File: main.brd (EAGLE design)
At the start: 81.3 x 100 mm, 8 parts, among them X1 FH12-40S-0.5SH

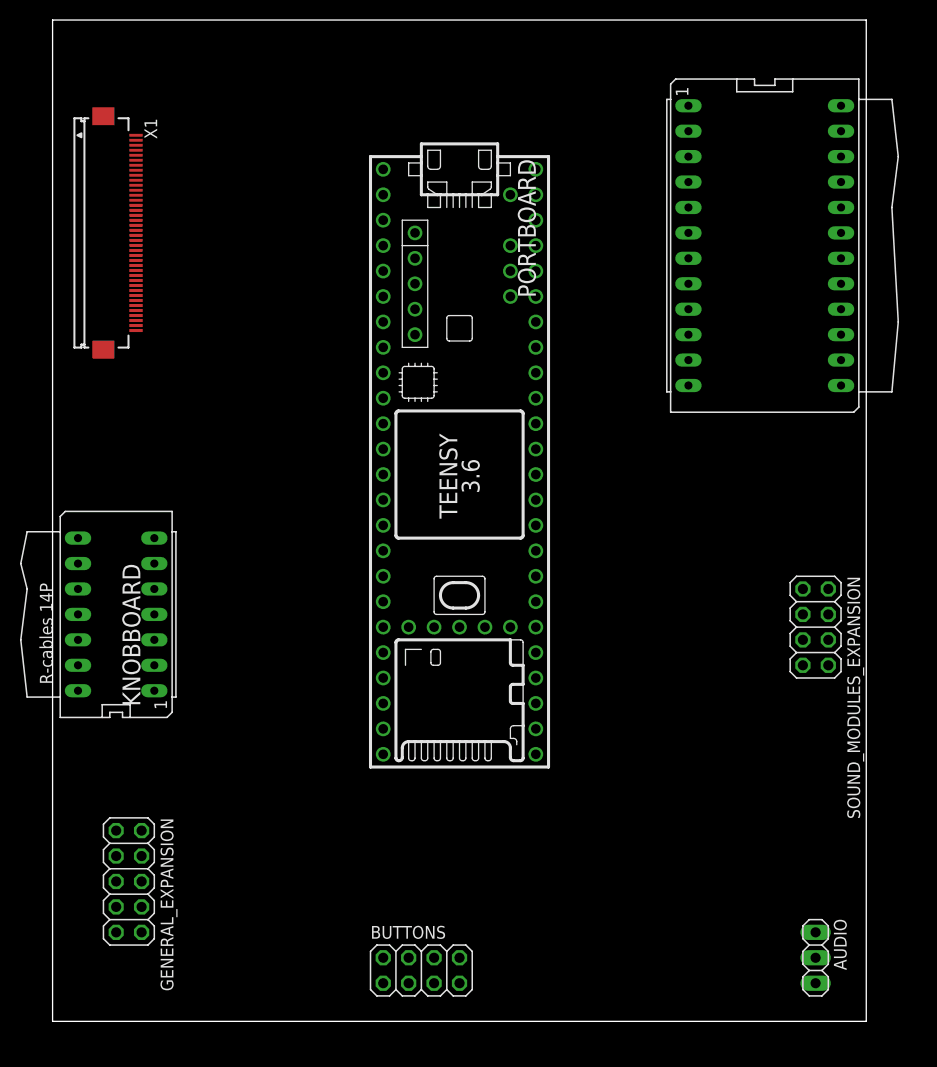
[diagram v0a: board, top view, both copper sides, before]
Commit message: pcb cleanup and audio_main tidy
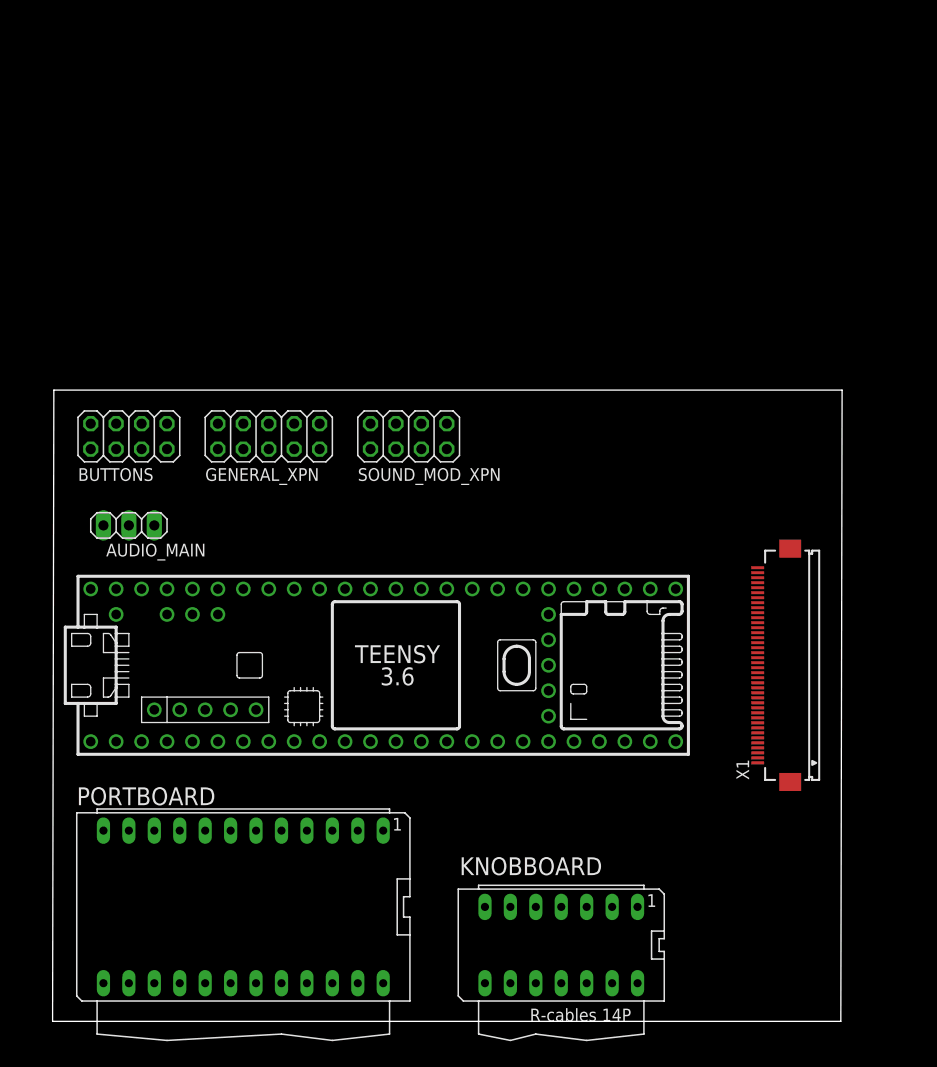
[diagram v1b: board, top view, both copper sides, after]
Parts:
- removed AUDIO: (no value), pinhead:1X03
- removed GENERAL_EXPANSION: (no value), pinhead:2X05
- removed SOUND_MODULES_EXPANSION: (no value), pinhead:2X04
- added AUDIO_MAIN: (no value), pinhead:1X03
- added GENERAL_XPN: (no value), pinhead:2X05
- added SOUND_MOD_XPN: (no value), pinhead:2X04
- moved PORTBOARD 84.1 mm to (19.1, 11.4), turned to 180 degrees
- moved X1 81.0 mm to (73.7, 35.6), turned to 90 degrees
- moved BUTTONS 60.8 mm to (7.62, 58.4)
- moved KNOBBOARD 55.4 mm to (50.8, 7.62), turned to 180 degrees
- moved U$1 23.3 mm to (31.8, 35.6), turned to 0 degrees
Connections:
- net AUDIO_GND: now also AUDIO_MAIN.2; no longer AUDIO.2
- net AUDIO_L: now also AUDIO_MAIN.1; no longer AUDIO.3
- net AUDIO_R: now also AUDIO_MAIN.3; no longer AUDIO.1
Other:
- board size 81.3 x 100 mm -> 78.8 x 63 mm

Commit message: general expansion slots
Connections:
- net N$10 renamed MIDIIN3
- net N$11 renamed MIDIIN4
- net N$12 renamed SDDATA1
- net N$3 renamed MIDIOUT1
- net N$4 renamed MIDIOUT2
- net N$5 renamed MIDIOUT3
- net N$6 renamed MIDIOUT4
- net N$7 renamed SDDATA0
- net N$8 renamed MIDIIN1
- net N$9 renamed MIDIIN2
- new net +12V: GENERAL_XPN.3
- new net BUTTON_CLK: BUTTONS.7
- new net BUTTON_DATA: BUTTONS.6
- new net BUTTON_S/P: BUTTONS.5
- new net LEDSCL: BUTTONS.4
- new net LED_SDA: BUTTONS.3
- new net SDCLK: PORTBOARD.9
- new net SDCMD: PORTBOARD.16
- new net SDDATA2: PORTBOARD.8
- new net SDDATA3: PORTBOARD.17
- new net SPI_CLK: GENERAL_XPN.8
- new net SPI_CS: GENERAL_XPN.7
- new net SPI_MISO: GENERAL_XPN.10
- new net SPI_MOSI: GENERAL_XPN.9
- net +3V3: now also BUTTONS.1
- net +5V: now also GENERAL_XPN.1
- net AUDIO_L: now also GENERAL_XPN.5
- net AUDIO_R: now also GENERAL_XPN.6
- net GND: now also BUTTONS.2, GENERAL_XPN.2
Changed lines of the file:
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@@
 <contactref element="PORTBOARD" pad="1"/>
 <contactref element="PORTBOARD" pad="2"/>
-<wire x1="70.41" y1="25.81" x2="58.42" y2="3.81" width="0" layer="19" extent="1-1"/>
-<wire x1="33.02" y1="19.05" x2="70.41" y2="25.81" width="0" layer="19" extent="1-1"/>
+<contactref element="BUTTONS" pad="2"/>
+<contactref element="GENERAL_XPN" pad="2"/>
+<wire x1="58.42" y1="3.81" x2="70.41" y2="25.81" width="0" layer="19" extent="1-1"/>
+<wire x1="33.02" y1="19.05" x2="58.42" y2="3.81" width="0" layer="19" extent="1-1"/>
 <wire x1="30.48" y1="19.05" x2="33.02" y2="19.05" width="0" layer="19" extent="1-1"/>
 <wire x1="3.81" y1="27.94" x2="30.48" y2="19.05" width="0" layer="19" extent="1-1"/>
+<wire x1="3.81" y1="59.69" x2="3.81" y2="27.94" width="0" layer="19" extent="1-1"/>
+<wire x1="16.51" y1="59.69" x2="3.81" y2="59.69" width="0" layer="19" extent="1-1"/>
 </signal>
 <signal name="+3V3">
 <contactref element="X1" pad="2"/>
-<contactref element="U$1" pad="3V3"/>
 <contactref element="KNOBBOARD" pad="1"/>
 <contactref element="PORTBOARD" pad="24"/>
-<wire x1="70.41" y1="26.31" x2="58.42" y2="11.43" width="0" layer="19" extent="1-1"/>
-<wire x1="33.02" y1="3.81" x2="70.41" y2="26.31" width="0" layer="19" extent="1-1"/>
-<wire x1="39.37" y1="27.94" x2="70.41" y2="26.31" width="0" layer="19" extent="1-1"/>
+<contactref element="U$1" pad="3V3"/>
+<contactref element="BUTTONS" pad="1"/>
+<wire x1="58.42" y1="11.43" x2="70.41" y2="26.31" width="0" layer="19" extent="1-1"/>
+<wire x1="39.37" y1="27.94" x2="58.42" y2="11.43" width="0" layer="19" extent="1-1"/>
+<wire x1="33.02" y1="3.81" x2="39.37" y2="27.94" width="0" layer="19" extent="1-1"/>
+<wire x1="3.81" y1="57.15" x2="39.37" y2="27.94" width="0" layer="19" extent="1-1"/>
 </signal>
 <signal name="+5V">
 <contactref element="U$1" pad="VIN"/>
 <contactref element="PORTBOARD" pad="23"/>
+<contactref element="GENERAL_XPN" pad="1"/>
+<wire x1="3.81" y1="43.18" x2="16.51" y2="57.15" width="0" layer="19" extent="1-1"/>
 <wire x1="30.48" y1="3.81" x2="3.81" y2="43.18" width="0" layer="19" extent="1-1"/>
 </signal>
@@
 <contactref element="U$1" pad="A22/DAC1"/>
 <contactref element="AUDIO_MAIN" pad="3"/>
-<wire x1="5.08" y1="49.53" x2="41.91" y2="43.18" width="0" layer="19" extent="1-1"/>
+<contactref element="GENERAL_XPN" pad="6"/>
+<wire x1="21.59" y1="59.69" x2="41.91" y2="43.18" width="0" layer="19" extent="1-1"/>
+<wire x1="5.08" y1="49.53" x2="21.59" y2="59.69" width="0" layer="19" extent="1-1"/>
 </signal>
 <signal name="AUDIO_L">
 <contactref element="U$1" pad="21/DAC0"/>
 <contactref element="AUDIO_MAIN" pad="1"/>
-<wire x1="10.16" y1="49.53" x2="44.45" y2="43.18" width="0" layer="19" extent="1-1"/>
+<contactref element="GENERAL_XPN" pad="5"/>
+<wire x1="21.59" y1="57.15" x2="44.45" y2="43.18" width="0" layer="19" extent="1-1"/>
+<wire x1="10.16" y1="49.53" x2="21.59" y2="57.15" width="0" layer="19" extent="1-1"/>
 </signal>
 <signal name="AUDIO_GND">
@@
 <wire x1="6.35" y1="43.18" x2="7.62" y2="49.53" width="0" layer="19" extent="1-1"/>
 </signal>
-<signal name="N$3">
+<signal name="MIDIOUT1">
 <contactref element="PORTBOARD" pad="3"/>
 </signal>
-<signal name="N$4">
+<signal name="MIDIOUT2">
 <contactref element="PORTBOARD" pad="4"/>
 </signal>
-<signal name="N$5">
+<signal name="MIDIOUT3">
 <contactref element="PORTBOARD" pad="5"/>
 </signal>
-<signal name="N$6">
+<signal name="MIDIOUT4">
 <contactref element="PORTBOARD" pad="6"/>
 </signal>
-<signal name="N$7">
+<signal name="SDDATA0">
 <contactref element="PORTBOARD" pad="7"/>
 </signal>
-<signal name="N$8">
+<signal name="MIDIIN1">
 <contactref element="PORTBOARD" pad="22"/>
 </signal>
-<signal name="N$9">
+<signal name="MIDIIN2">
 <contactref element="PORTBOARD" pad="21"/>
 </signal>
-<signal name="N$10">
+<signal name="MIDIIN3">
 <contactref element="PORTBOARD" pad="20"/>
 </signal>
-<signal name="N$11">
+<signal name="MIDIIN4">
 <contactref element="PORTBOARD" pad="19"/>
 </signal>
-<signal name="N$12">
+<signal name="SDDATA1">
 <contactref element="PORTBOARD" pad="18"/>
 </signal>
+<signal name="SDDATA2">
+<contactref element="PORTBOARD" pad="8"/>
+</signal>
+<signal name="SDCLK">
+<contactref element="PORTBOARD" pad="9"/>
+</signal>
+<signal name="SDDATA3">
+<contactref element="PORTBOARD" pad="17"/>
+</signal>
+<signal name="SDCMD">
+<contactref element="PORTBOARD" pad="16"/>
+</signal>
+<signal name="LED_SDA">
+<contactref element="BUTTONS" pad="3"/>
+</signal>
+<signal name="BUTTON_S/P">
+<contactref element="BUTTONS" pad="5"/>
+</signal>
+<signal name="BUTTON_CLK">
+<contactref element="BUTTONS" pad="7"/>
+</signal>
+<signal name="LEDSCL">
+<contactref element="BUTTONS" pad="4"/>
+</signal>
+<signal name="BUTTON_DATA">
+<contactref element="BUTTONS" pad="6"/>
+</signal>
+<signal name="SPI_CS">
+<contactref element="GENERAL_XPN" pad="7"/>
+</signal>
+<signal name="SPI_CLK">
+<contactref element="GENERAL_XPN" pad="8"/>
+</signal>
+<signal name="SPI_MOSI">
+<contactref element="GENERAL_XPN" pad="9"/>
+</signal>
+<signal name="SPI_MISO">
+<contactref element="GENERAL_XPN" pad="10"/>
+</signal>
+<signal name="+12V">
+<contactref element="GENERAL_XPN" pad="3"/>
+</signal>
 </signals>

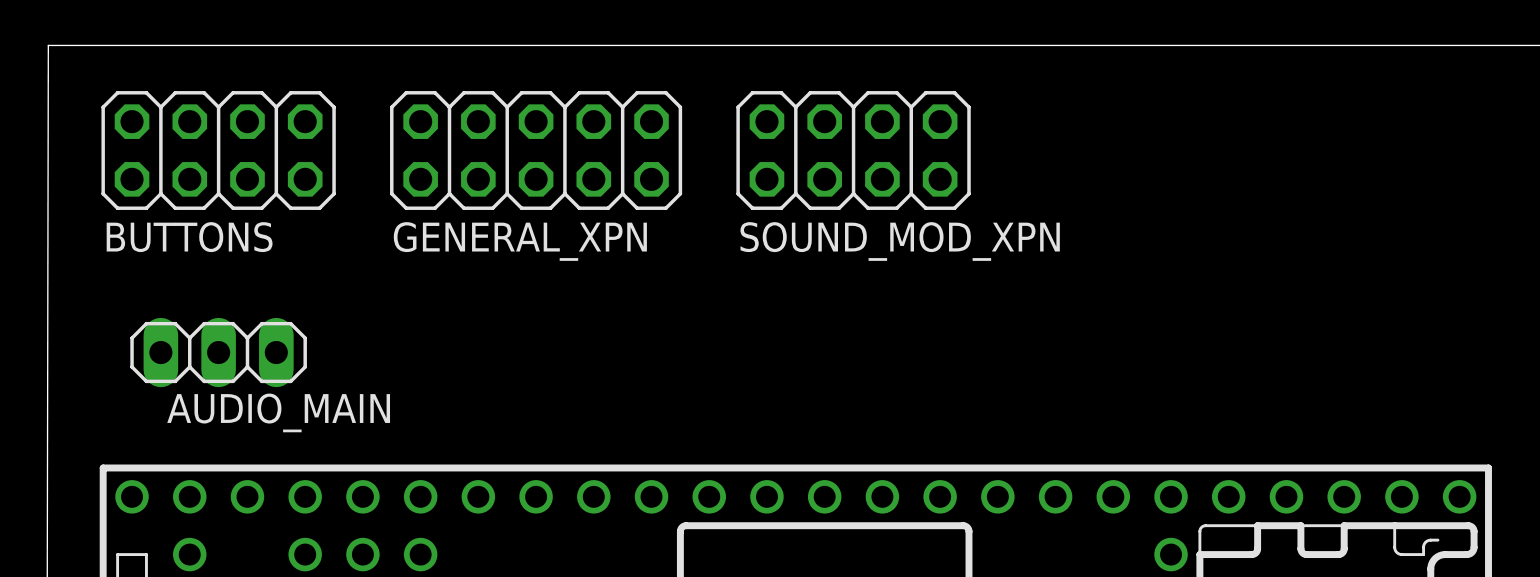
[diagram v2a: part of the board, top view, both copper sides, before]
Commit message: MIDI pinout connections, backup files cleanup, gitignore
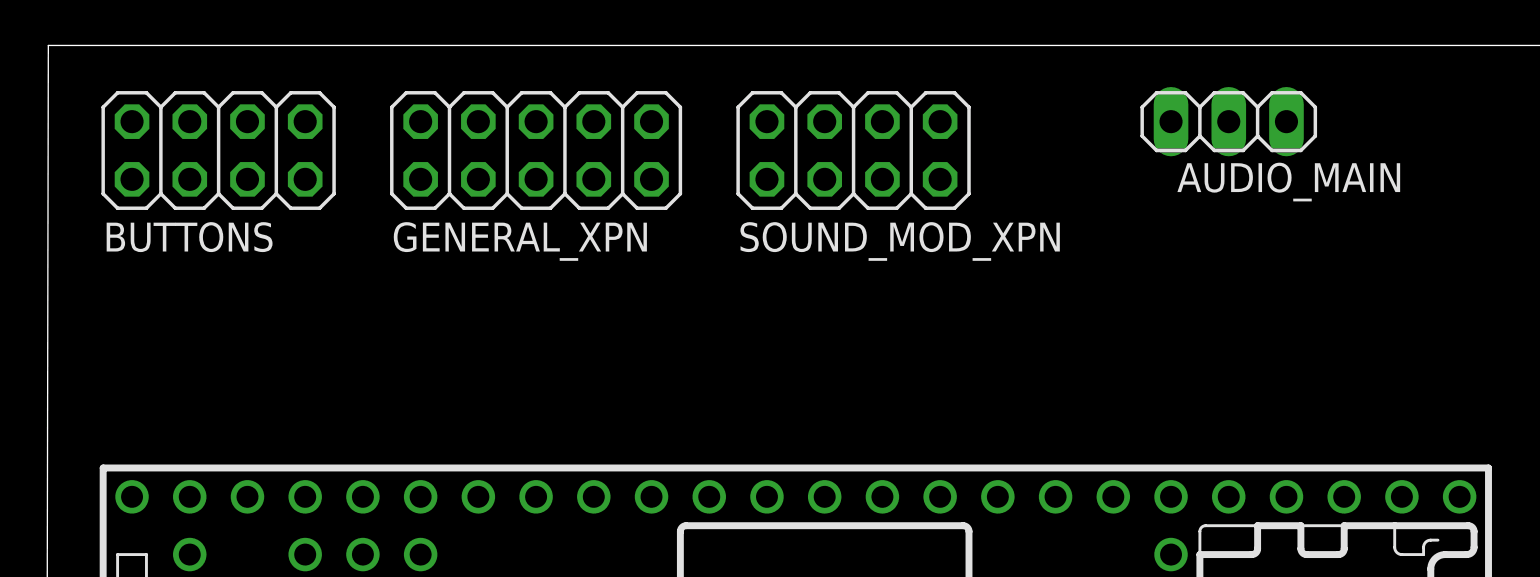
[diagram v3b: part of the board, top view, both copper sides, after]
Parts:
- moved AUDIO_MAIN 45.6 mm to (52.1, 59.7)
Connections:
- new net N$10: U$1.25
- new net N$11: U$1.26
- new net N$12: U$1.27
- new net N$13: U$1.28
- new net N$14: U$1.29
- new net N$15: U$1.30
- new net N$18: U$1.23/A9
- new net N$19: U$1.22/A8
- new net N$20: U$1.21/A7
- new net N$21: U$1.20/A6
- new net N$22: U$1.19/A5/SCL
- new net N$23: U$1.18/A4/SDA
- new net N$24: U$1.17/A3
- new net N$25: U$1.15/A1
- new net N$26: U$1.14/A0
- new net N$3: U$1.2
- new net N$30: U$1.35/A16
- new net N$31: U$1.36/A17
- new net N$32: U$1.37/A18
- new net N$33: U$1.38/A19
- new net N$34: U$1.39/A20
- new net N$4: U$1.3/CANTX
- new net N$5: U$1.4/CANRX
- new net N$6: U$1.6
- new net N$9: U$1.24
- net MIDIIN1: now also U$1.0/RX
- net MIDIIN2: now also U$1.7
- net MIDIIN3: now also U$1.31/A12
- net MIDIIN4: now also U$1.34/A15
- net MIDIOUT1: now also U$1.1/TX
- net MIDIOUT2: now also U$1.8
- net MIDIOUT3: now also U$1.32/A13
- net MIDIOUT4: now also U$1.33/A14
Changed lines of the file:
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@@
 <attribute name="VALUE" x="73.9858" y="25.3124" size="1.27" layer="27" rot="R90"/>
 </element>
-<element name="AUDIO_MAIN" library="pinhead" library_urn="urn:adsk.eagle:library:325" package="1X03" package3d_urn="urn:adsk.eagle:package:22458/2" value="" x="7.62" y="49.53" smashed="yes" rot="R180">
-<attribute name="NAME" x="15.3162" y="47.7012" size="1.27" layer="25" ratio="10" rot="R180"/>
-<attribute name="POPULARITY" value="92" x="7.62" y="49.53" size="1.778" layer="27" rot="R180" display="off"/>
-<attribute name="VALUE" x="11.43" y="52.705" size="1.27" layer="27" rot="R180"/>
+<element name="AUDIO_MAIN" library="pinhead" library_urn="urn:adsk.eagle:library:325" package="1X03" package3d_urn="urn:adsk.eagle:package:22458/2" value="" x="52.07" y="59.69" smashed="yes" rot="R180">
+<attribute name="NAME" x="59.7662" y="57.8612" size="1.27" layer="25" ratio="10" rot="R180"/>
+<attribute name="POPULARITY" value="92" x="52.07" y="59.69" size="1.778" layer="27" rot="R180" display="off"/>
+<attribute name="VALUE" x="55.88" y="62.865" size="1.27" layer="27" rot="R180"/>
 </element>
 </elements>
@@
 <contactref element="GENERAL_XPN" pad="6"/>
 <wire x1="21.59" y1="59.69" x2="41.91" y2="43.18" width="0" layer="19" extent="1-1"/>
-<wire x1="5.08" y1="49.53" x2="21.59" y2="59.69" width="0" layer="19" extent="1-1"/>
+<wire x1="49.53" y1="59.69" x2="21.59" y2="59.69" width="0" layer="19" extent="1-1"/>
 </signal>
 <signal name="AUDIO_L">
@@
 <contactref element="GENERAL_XPN" pad="5"/>
 <wire x1="21.59" y1="57.15" x2="44.45" y2="43.18" width="0" layer="19" extent="1-1"/>
-<wire x1="10.16" y1="49.53" x2="21.59" y2="57.15" width="0" layer="19" extent="1-1"/>
+<wire x1="54.61" y1="59.69" x2="21.59" y2="57.15" width="0" layer="19" extent="1-1"/>
 </signal>
 <signal name="AUDIO_GND">
 <contactref element="U$1" pad="AGND"/>
 <contactref element="AUDIO_MAIN" pad="2"/>
-<wire x1="6.35" y1="43.18" x2="7.62" y2="49.53" width="0" layer="19" extent="1-1"/>
+<wire x1="6.35" y1="43.18" x2="52.07" y2="59.69" width="0" layer="19" extent="1-1"/>
 </signal>
 <signal name="MIDIOUT1">
 <contactref element="PORTBOARD" pad="3"/>
+<contactref element="U$1" pad="1/TX"/>
+<wire x1="8.89" y1="27.94" x2="27.94" y2="19.05" width="0" layer="19" extent="1-1"/>
 </signal>
 <signal name="MIDIOUT2">
 <contactref element="PORTBOARD" pad="4"/>
+<contactref element="U$1" pad="8"/>
+<wire x1="25.4" y1="19.05" x2="26.67" y2="27.94" width="0" layer="19" extent="1-1"/>
 </signal>
 <signal name="MIDIOUT3">
 <contactref element="PORTBOARD" pad="5"/>
+<contactref element="U$1" pad="32/A13"/>
+<wire x1="22.86" y1="19.05" x2="62.23" y2="27.94" width="0" layer="19" extent="1-1"/>
 </signal>
 <signal name="MIDIOUT4">
 <contactref element="PORTBOARD" pad="6"/>
+<contactref element="U$1" pad="33/A14"/>
+<wire x1="20.32" y1="19.05" x2="62.23" y2="43.18" width="0" layer="19" extent="1-1"/>
 </signal>
 <signal name="SDDATA0">
@@
 <signal name="MIDIIN1">
 <contactref element="PORTBOARD" pad="22"/>
+<contactref element="U$1" pad="0/RX"/>
+<wire x1="27.94" y1="3.81" x2="6.35" y2="27.94" width="0" layer="19" extent="1-1"/>
 </signal>
 <signal name="MIDIIN2">
 <contactref element="PORTBOARD" pad="21"/>
+<contactref element="U$1" pad="7"/>
+<wire x1="25.4" y1="3.81" x2="24.13" y2="27.94" width="0" layer="19" extent="1-1"/>
 </signal>
 <signal name="MIDIIN3">
 <contactref element="PORTBOARD" pad="20"/>
+<contactref element="U$1" pad="31/A12"/>
+<wire x1="22.86" y1="3.81" x2="59.69" y2="27.94" width="0" layer="19" extent="1-1"/>
 </signal>
 <signal name="MIDIIN4">
 <contactref element="PORTBOARD" pad="19"/>
+<contactref element="U$1" pad="34/A15"/>
+<wire x1="20.32" y1="3.81" x2="59.69" y2="43.18" width="0" layer="19" extent="1-1"/>
 </signal>
 <signal name="SDDATA1">
@@
 <contactref element="GENERAL_XPN" pad="3"/>
 </signal>
+<signal name="N$3">
+<contactref element="U$1" pad="2"/>
+</signal>
+<signal name="N$4">
+<contactref element="U$1" pad="3/CANTX"/>
+</signal>
+<signal name="N$5">
+<contactref element="U$1" pad="4/CANRX"/>
+</signal>
+<signal name="N$6">
+<contactref element="U$1" pad="6"/>
+</signal>
+<signal name="N$9">
+<contactref element="U$1" pad="24"/>
+</signal>
+<signal name="N$10">
+<contactref element="U$1" pad="25"/>
+</signal>
+<signal name="N$11">
+<contactref element="U$1" pad="26"/>
+</signal>
+<signal name="N$12">
+<contactref element="U$1" pad="27"/>
+</signal>
+<signal name="N$13">
+<contactref element="U$1" pad="28"/>
+</signal>
+<signal name="N$14">
+<contactref element="U$1" pad="29"/>
+</signal>
+<signal name="N$15">
+<contactref element="U$1" pad="30"/>
+</signal>
+<signal name="N$18">
+<contactref element="U$1" pad="23/A9"/>
+</signal>
+<signal name="N$19">
+<contactref element="U$1" pad="22/A8"/>
+</signal>
+<signal name="N$20">
+<contactref element="U$1" pad="21/A7"/>
+</signal>
+<signal name="N$21">
+<contactref element="U$1" pad="20/A6"/>
+</signal>
+<signal name="N$22">
+<contactref element="U$1" pad="19/A5/SCL"/>
+</signal>
+<signal name="N$23">
+<contactref element="U$1" pad="18/A4/SDA"/>
+</signal>
+<signal name="N$24">
+<contactref element="U$1" pad="17/A3"/>
+</signal>
+<signal name="N$25">
+<contactref element="U$1" pad="15/A1"/>
+</signal>
+<signal name="N$26">
+<contactref element="U$1" pad="14/A0"/>
+</signal>
+<signal name="N$30">
+<contactref element="U$1" pad="35/A16"/>
+</signal>
+<signal name="N$31">
+<contactref element="U$1" pad="36/A17"/>
+</signal>
+<signal name="N$32">
+<contactref element="U$1" pad="37/A18"/>
+</signal>
+<signal name="N$33">
+<contactref element="U$1" pad="38/A19"/>
+</signal>
+<signal name="N$34">
+<contactref element="U$1" pad="39/A20"/>
+</signal>
 </signals>
